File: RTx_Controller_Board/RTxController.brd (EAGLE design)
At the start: 101.6 x 85.5 mm, 124 parts, among them IC1 LTC4263, IC2 TLK110", Q1 25MHz, U2 TPD4S012, X4 MINI-USB-32005-301

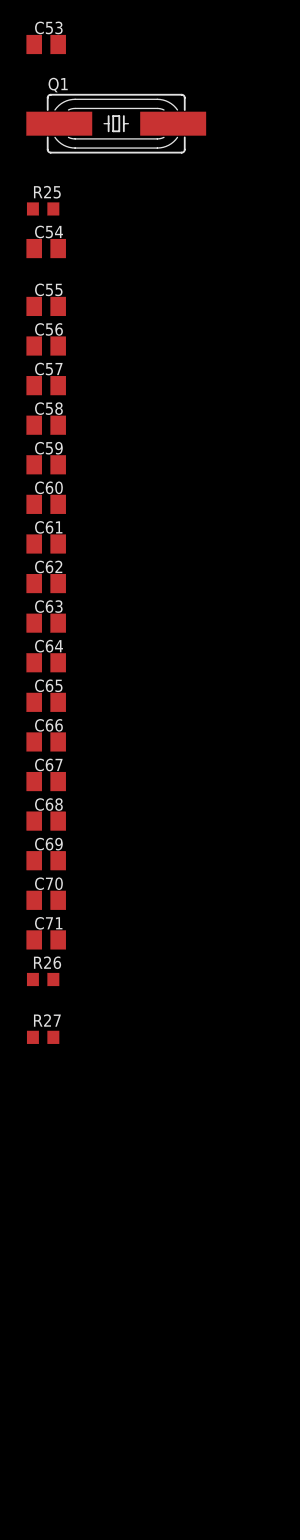
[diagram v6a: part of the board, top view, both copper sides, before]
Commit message: Added Ethernet pinouts to MCU.
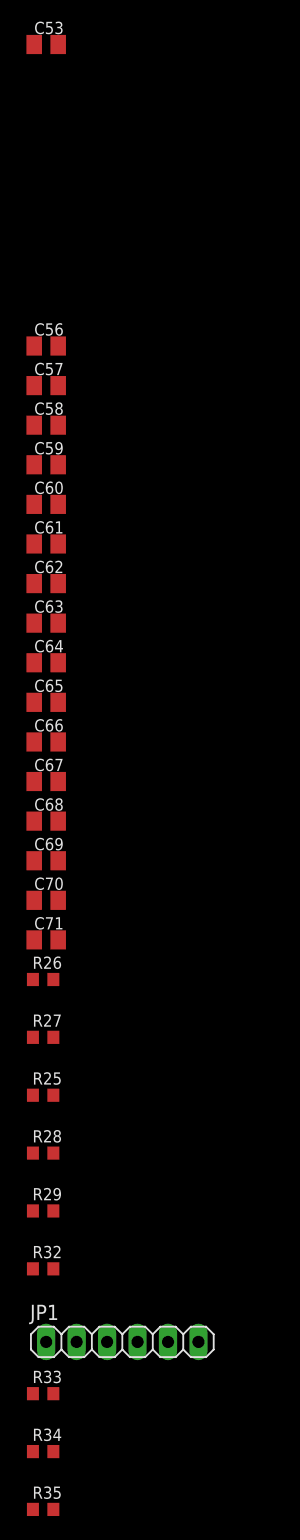
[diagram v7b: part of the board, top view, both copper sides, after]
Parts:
- removed C54, C55: (no value), motorFeedback:C0805K
- removed Q1: 25MHz, motorFeedback:CSM-7X
- added JP1: (no value), motorFeedback:1X06
- added R28: 470, motorFeedback:R0603
- added R29, R32: 2.2k, motorFeedback:R0603
- added R33, R34, R35: 1k, motorFeedback:R0603
- R25: value (none) -> 470
- moved R25 73.9 mm to (-88.6, -379.5)
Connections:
- net 48VDC+ renamed DC+
- net 48VDC- renamed DC-
- new net N$35: R25.2, U$6.17
- new net N$36: IC2.27, R28.1, R32.1
- new net N$37: IC2.29, R34.1
- new net N$38: IC2.7, R35.1
- new net N$56: IC2.8, JP1.1
- new net N$57: IC2.12, JP1.2
- new net N$58: IC2.9, JP1.3
- new net N$59: IC2.10, JP1.4
- new net N$60: IC2.11, JP1.5
- new net PA1/ETH_MII_RX_CLK: IC2.38
- new net PA2/ETH_MDIO: IC2.30
- new net PA7/ETH_MII_RX_DV: IC2.39
- new net PA8/MCO1: IC2.34
- new net PB0/ETH_MII_RXD2: IC2.45
- new net PB1/ETH_MII_RXD3: IC2.46
- new net PB10/ETH_MII_RX_ER: IC2.41
- new net PB8/ETH_MII_TXD3: IC2.6
- new net PC1/ETH_MDC: IC2.31
- new net PC2/ETH_MII_TXD2: IC2.5
- new net PC3/ETH_MII_TX_CLK: IC2.1
- new net PC4/ETH_MII_RXDO: IC2.43
- new net PC5/ETH_MII_RXD1: IC2.44
- new net PG11/ETH_MII_TX_EN: IC2.2
- new net PG13/ETH_MII_TXD0: IC2.3
- new net PG14/ETH_MII_TXD1: IC2.4
- new net PH2/ETH_MII_CRS: IC2.40
- new net PH3/ETH_MII_COL: IC2.42
- net +3.3V: now also R33.2, R34.2, R35.2
- net GND: now also R29.2, R32.2, U$6.18, U$6.20; no longer C54.2, C55.2
- net N$31: now also IC2.21, R33.1; no longer IC2.33, R25.2
- net N$32: now also R28.2, U$6.19; no longer C55.1, IC2.34, Q1.1
- net N$33: now also IC2.28, R29.1; no longer C54.1, Q1.2

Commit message: Added CPU to schematic, completed pin-out of GMD signals, Ethernet signals, USB signals. Needs JTAG connector, ESD protection.
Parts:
- added C100, C101, C102, C103, C104, C105, C106, C107, C108, C109, C110, C111, C112, C113, C114, C115, C116, C117, C118, C119, C120, C121, C122, C123, C124, C93, C94, C95, C96, C97, C98, C99: (no value), motorFeedback:C0603
- added C54, C55, C72, C73, C74, C75, C76, C77, C78, C79, C80, C81, C82, C83, C84, C88, C90, C92: 0.1u, motorFeedback:C0402
- added C85: 4.7u, motorFeedback:C0603
- added C86, C87: 2.2u, motorFeedback:C0402
- added C89, C91: 1.0u, motorFeedback:C0402
- added R36: 0, motorFeedback:R0603
- added R37, R39, R40, R41, R42, R43, R44, R45, R46, R47, R48, R49, R50, R51, R52, R53: (no value), motorFeedback:R0603
- added R38: 10k, motorFeedback:R0603
- added SW1: COM08720, motorFeedback:COM08720
- added U1: STM32F407ZXT, motorFeedback:LQFP-100
- added X3: (no value), con-subd:HDF15H
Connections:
- removed net CNV: ADC1.6, ADC1.9, ADC2.6, ADC3.6, ADC4.6
- removed net PA1/ETH_MII_RX_CLK: IC2.38
- removed net PA10/ID: U2.3, X4.4
- removed net PA11/D-: R21.2
- removed net PA12/D+: R22.2
- removed net PA2/ETH_MDIO: IC2.30
- removed net PA7/ETH_MII_RX_DV: IC2.39
- removed net PA8/MCO1: IC2.34
- removed net PA9/BBUS: C45.1, C46.1, U2.6, X4.1
- removed net PB0/ETH_MII_RXD2: IC2.45
- removed net PB1/ETH_MII_RXD3: IC2.46
- removed net PB10/ETH_MII_RX_ER: IC2.41
- removed net PB8/ETH_MII_TXD3: IC2.6
- removed net PC1/ETH_MDC: IC2.31
- removed net PC2/ETH_MII_TXD2: IC2.5
- removed net PC3/ETH_MII_TX_CLK: IC2.1
- removed net PC4/ETH_MII_RXDO: IC2.43
- removed net PC5/ETH_MII_RXD1: IC2.44
- removed net PG11/ETH_MII_TX_EN: IC2.2
- removed net PG13/ETH_MII_TXD0: IC2.3
- removed net PG14/ETH_MII_TXD1: IC2.4
- removed net PH2/ETH_MII_CRS: IC2.40
- removed net PH3/ETH_MII_COL: IC2.42
- removed net SCK: ADC1.8, ADC2.8, ADC3.8, ADC4.8
- removed net SDO: R16.2, R20.2
- new net ENABLE_AXIS3_OUT: C116.1, R46.2, U1.81
- new net ENABLE_AXIS4_OUT: C114.1, R48.2, U1.83
- new net ENABLE_LAT_OUT: C107.1, R43.2, U1.58
- new net ENABLE_VERT_OUT: C105.1, R45.2, U1.87
- new net ETH_MCO1: IC2.34, U1.67
- new net ETH_MDC: IC2.31, U1.16
- new net ETH_MDIO: IC2.30, U1.25
- new net ETH_MII_COL: IC2.42, U1.26
- new net ETH_MII_CRS: IC2.40, U1.23
- new net ETH_MII_RXD0: IC2.43, U1.33
- new net ETH_MII_RXD1: IC2.44, U1.34
- new net ETH_MII_RXD2: IC2.45, U1.35
- new net ETH_MII_RXD3: IC2.46, U1.36
- new net ETH_MII_RX_CLK: IC2.38, U1.24
- new net ETH_MII_RX_DV: IC2.39, U1.32
- new net ETH_MII_RX_ER: IC2.41, U1.47
- new net ETH_MII_TXD0: IC2.3, U1.51
- new net ETH_MII_TXD1: IC2.4, U1.52
- new net ETH_MII_TXD2: IC2.5, U1.17
- new net ETH_MII_TXD3: IC2.6, U1.95
- new net ETH_MII_TX_CLK: IC2.1, U1.18
- new net ETH_MII_TX_EN: IC2.2, U1.48
- new net N$39: C92.1, SW1.1, SW1.3, U1.14
- new net N$42: C96.1, R37.1, X2.15
- new net N$43: R36.2, U1.6
- new net N$44: R38.1, U1.94
- new net N$45: C95.1, R39.1, X2.14
- new net N$46: C94.1, R40.1, X2.13
- new net N$47: C93.1, R41.1, X2.12
- new net N$48: C104.1, R42.1, X2.4
- new net N$49: C103.1, R43.1, X2.3
- new net N$50: C102.1, R44.1, X2.2
- new net N$51: C101.1, R45.1, X2.1
- new net N$52: C112.1, R46.1, X3.4
- new net N$53: C111.1, R47.1, X3.3
- new net N$54: C110.1, R48.1, X3.2
- new net N$55: C109.1, R49.1, X3.1
- new net N$61: C120.1, R50.1, X3.15
- new net N$62: C119.1, R51.1, X3.14
- new net N$63: C118.1, R52.1, X3.13
- new net N$64: C117.1, R53.1, X3.12
- new net PWM_AXIS3_U_OUT: C123.1, R51.2, U1.64
- new net PWM_AXIS3_V_OUT: C124.1, R50.2, U1.63
- new net PWM_AXIS4_U_OUT: C121.1, R53.2, U1.66
- new net PWM_AXIS4_V_OUT: C122.1, R52.2, U1.65
- new net PWM_LAT_U_OUT: C97.1, R41.2, U1.62
- new net PWM_LAT_V_OUT: C98.1, R40.2, U1.61
- new net PWM_VERT_U_OUT: C99.1, R39.2, U1.60
- new net PWM_VERT_V_OUT: C100.1, R37.2, U1.59
- new net SPI_MISO: R16.2, R20.2, U1.31
- new net SPI_MOSI: ADC1.6, ADC1.9, ADC2.6, ADC3.6, ADC4.6, U1.91
- new net SPI_NCS: U1.29
- new net SPI_SCK: ADC1.8, ADC2.8, ADC3.8, ADC4.8, U1.30
- new net USB_D+: R22.2, U1.71
- new net USB_D-: R21.2, U1.70
- new net USB_ID: U1.69, U2.3, X4.4
- new net USB_VBUS: C45.1, C46.1, U1.68, U2.6, X4.1
- new net VCAP_1@49: C87.1, U1.49
- new net VCAP_2@73: C86.1, U1.73
- new net VDDA@22: C88.1, C89.1, C90.1, C91.1, U1.21, U1.22
- new net WATCHDOG_AXIS3_OUT: C115.1, R47.2, U1.82
- new net WATCHDOG_AXIS4_OUT: C113.1, R49.2, U1.84
- new net WATCHDOG_LAT_OUT: C108.1, R42.2, U1.57
- new net WATCHDOG_VERT_OUT: C106.1, R44.2, U1.86
- net +3.3V: now also C54.1, C55.1, C72.1, C73.1, C74.1, C75.1, C76.1, C77.1, C78.1, C79.1, C80.1, C81.1, C82.1, C83.1, C84.1, C85.1, R36.1, U1.100, U1.11, U1.19, U1.28, U1.50, U1.75
- net GND: now also C100.2, C101.2, C102.2, C103.2, C104.2, C105.2, C106.2, C107.2, C108.2, C109.2, C110.2, C111.2, C112.2, C113.2, C114.2, C115.2, C116.2, C117.2, C118.2, C119.2, C120.2, C121.2, C122.2, C123.2, C124.2, C54.2, C55.2, C72.2, C73.2, C74.2, C75.2, C76.2, C77.2, C78.2, C79.2, C80.2, C81.2, C82.2, C83.2, C84.2, C85.2, C86.2, C87.2, C88.2, C89.2, C90.2, C91.2, C92.2, C93.2, C94.2, C95.2, C96.2, C97.2, C98.2, C99.2, JP1.6, R38.2, SW1.2, SW1.4, U1.10, U1.20, U1.27, U1.74, U1.99, X2.10, X2.5, X2.6, X2.7, X2.8, X3.10, X3.5, X3.6, X3.7, X3.8
